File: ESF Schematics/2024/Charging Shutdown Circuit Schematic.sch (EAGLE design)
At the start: 33 parts, among them J1 CONNECTOR-1_6MM2, J10 CONNECTOR-1_CT2242-2, J11 CONNECTOR-5_1-2393947-1, J12 CONNECTOR-3_XXC106-EV-P3Z, J15 CONNECTOR-3_NEMA-5-20, J16 CONNECTOR-3_NEMA-5-20, J17 CONNECTOR-2_, J18 CONNECTOR-2_, J2 CONNECTOR-1_LCAX2-14F-E, J3 CONNECTOR-1_6MM2, J4 CONNECTOR-1_LCAX2-14F-E, J5 CONNECTOR-3_XXC106-EV-P3Z, J6 RING_TERMINAL_19054-0042, J7 RING_TERMINAL_19054-0042, J8 CONNECTOR-3_NEMA-5-20, J9 CONNECTOR-1_CT2242-2

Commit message: num num
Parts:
- removed F3: 175A, HyTechSymbolsTemp:FUSE
- removed F4, F5: 1A, HyTechSymbolsTemp:FUSE
- removed J12, U$3: CONNECTOR-3_XXC106-EV-P3Z, HyTechSymbols:CONNECTOR-3_XXC106-EV-P3Z
- removed J18: CONNECTOR-2_, HyTechSymbols:CONNECTOR-2_XXC104-EV-P1ZA
- removed R1, R2: 15k, HyTechSymbolsTemp:RESISTOR
- removed S2: SWITCH_SPST_, HyTechSymbols:SWITCH_SPST_
- removed U$1, U$4: CONNECTOR-2_HVP800, HyTechSymbols:CONNECTOR-2_HVP800
- removed U$15: CHARGER_CONTROLLER, HyTechSymbolsTemp:CHARGER_CONTROLLER
- removed U$5: BENDER_IR155-3204, HyTechSymbols:BENDER_IR155-3204
- removed U$6: RING_TERMINAL_19054-0042, HyTechSymbolsTemp:RING_TERMINAL_19054-0042
- added AIR+, AIR-: RELAY_SPST_NO_, HyTechSymbols:RELAY_SPST_NO_
- added AMS_RELAY, IMD_RELAY, SOFTWARE_SHDN_RELAY: RELAY_DPDT_RT424024, HyTechSymbols:RELAY_DPDT_RT424024
- added D1, D2, D3, D5, D6, D7: DIODE, HyTechSymbolsTemp:DIODE
- added F1: 3A, HyTechSymbolsTemp:FUSE
- added J14: CONNECTOR-3_NEMA-5-20, HyTechSymbolsTemp:CONNECTOR-3_NEMA-5-20
- added LATCHING_BUTTON: BUTTON_NO_LP9, HyTechSymbolsTemp:BUTTON_NO_LP9
- added S3: SWITCH_SPST_, HyTechSymbols:SWITCH_SPST_
- added U$11: CHARGER_CONTROLLER, HyTechSymbolsTemp:CHARGER_CONTROLLER
- added U$12: BENDER_IR155-3204, HyTechSymbols:BENDER_IR155-3204
- A1: value REMOTE_POWER_CONTROL_RPC-20-SCD -> INLINE_GFCI_GFM20-3WC; device HyTechSymbolsTemp:REMOTE_POWER_CONTROL_RPC-20-SCD -> HyTechSymbolsTemp:INLINE_GFCI_GFM20-3WC
- A2: value CHARGER_HK-J-H650-12 -> REMOTE_POWER_CONTROL_RPC-20-SCD; device HyTechSymbols:CHARGER_HK-J-H650-12 -> HyTechSymbolsTemp:REMOTE_POWER_CONTROL_RPC-20-SCD
- A3: value INLINE_GFCI_GFM20-3WC -> CHARGER_HK-J-H650-12; device HyTechSymbolsTemp:INLINE_GFCI_GFM20-3WC -> HyTechSymbols:CHARGER_HK-J-H650-12
- J10, J9: value CONNECTOR-1_CT2242-2 -> CONNECTOR-3_XXC106-EV-P3Z; device HyTechSymbolsTemp:CONNECTOR-1_CT2242-2 -> HyTechSymbols:CONNECTOR-3_XXC106-EV-P3Z
- J16: value CONNECTOR-3_NEMA-5-20 -> CONNECTOR-2_; device HyTechSymbolsTemp:CONNECTOR-3_NEMA-5-20 -> HyTechSymbols:CONNECTOR-2_XXC104-EV-P1ZA
- J2: value CONNECTOR-1_LCAX2-14F-E -> CONNECTOR-1_6MM2; device HyTechSymbols:CONNECTOR-1_LCAX2-14F-E -> HyTechSymbols:CONNECTOR-1_6MM2
- J3: value CONNECTOR-1_6MM2 -> CONNECTOR-2_HVP800; device HyTechSymbols:CONNECTOR-1_6MM2 -> HyTechSymbols:CONNECTOR-2_HVP800
- J5: value CONNECTOR-3_XXC106-EV-P3Z -> CONNECTOR-2_HVP800; device HyTechSymbols:CONNECTOR-3_XXC106-EV-P3Z -> HyTechSymbols:CONNECTOR-2_HVP800
- J6: value RING_TERMINAL_19054-0042 -> CONNECTOR-1_LCAX2-14F-E; device HyTechSymbols:RING_TERMINAL_19054-0042 -> HyTechSymbols:CONNECTOR-1_LCAX2-14F-E
- J7: value RING_TERMINAL_19054-0042 -> CONNECTOR-3_NEMA-5-20; device HyTechSymbols:RING_TERMINAL_19054-0042 -> HyTechSymbolsTemp:CONNECTOR-3_NEMA-5-20
- J8: value CONNECTOR-3_NEMA-5-20 -> CONNECTOR-3_XXC106-EV-P3Z; device HyTechSymbolsTemp:CONNECTOR-3_NEMA-5-20 -> HyTechSymbols:CONNECTOR-3_XXC106-EV-P3Z
- S1: MPN AIR+ -> CHARGER_SHUTDOWN_BTN
- U$7: value RING_TERMINAL_19054-0042 -> PRECHARGER; device HyTechSymbolsTemp:RING_TERMINAL_19054-0042 -> HyTechSymbolsTemp:PRECHARGER
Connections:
- removed net N$27: R2.1, U$6.P$2
- removed net N$28: A3.HOT_OUT, J8.1
- removed net N$29: A3.GND_OUT, J8.3
- removed net N$30: A3.GND_IN, J16.3
- removed net N$35 (its old number): F4.2, J6.P$2
- removed net N$36 (its old number): F3.2, S2.P
- removed net N$37 (its old number): J11.3, J12.2
- removed net N$9: J10.1, R2.2
- removed net OKHS: U$5.OKHS
- new net AMS_OK: AMS_RELAY.COIL+, D1.C
- new net IMD_OK: D2.C, IMD_RELAY.COIL+, U$12.OKHS
- new net N$13: AIR-.CONTACT2, J5.1, U$7.TS-
- new net N$16: J1.1, J17.1
- new net N$17: J17.2, J2.1
- new net N$18: J10.3, J11.4
- new net N$22: A3.GND, J8.3
- new net N$24: A2.NEUTRAL_IN, J7.2
- new net N$33: A2.GND_OUT, J9.1
- new net N$34: A1.GND_OUT, J14.3
- new net N$40: A3.TS-, J16.2
- new net N$41: J10.1, J11.2
- new net PACK+: AIR+.CONTACT2, U$7.PACK+
- new net PACK-: AIR-.CONTACT1
- new net PRECHARGE_OK: AIR+.COIL-, U$7.PRECHARGE_OK
- new net SOFTWARE_OK: D3.C, SOFTWARE_SHDN_RELAY.COIL+
- net +12V: now also F1.1, U$12.+12V; no longer U$5.+12V
- net CHARGER_CONTROLLER_CANH: now also A3.CANH, U$11.CANH; no longer A2.CANH, U$15.CANH
- net CHARGER_CONTROLLER_CANL: now also A3.CANL, U$11.CANL; no longer A2.CANL, U$15.CANL
- net GND: now also AIR+.COIL+, AIR-.COIL+, AMS_RELAY.4, IMD_RELAY.4, LATCHING_BUTTON.P$2, SOFTWARE_SHDN_RELAY.4, U$12.GND, U$7.GND; no longer U$5.GND
- net N$1: now also D2.A, D7.A, IMD_RELAY.3, IMD_RELAY.COIL-; no longer A2.NEUTRAL, U$3.2
- net N$10: now also AMS_RELAY.5, SOFTWARE_SHDN_RELAY.6; no longer S1.P, U$1.1
- net N$11: now also AMS_RELAY.6, IMD_RELAY.5; no longer F3.1, U$1.2
- net N$12: now also AIR+.CONTACT1, J5.2, U$7.TS+; no longer J11.2, J12.1
- net N$14: now also J3.1, J6.1; no longer J1.1, J18.1
- net N$15: now also A2.HOT_OUT, J9.3; no longer J18.2, J3.1
- net N$19: now also J10.2, J11.3; no longer A1.GND_OUT, J5.3
- net N$2: now also D5.C, D6.C, D7.C, LATCHING_BUTTON.P$1; no longer A2.GND, U$3.3
- net N$20: now also A3.HOT, J8.1; no longer J4.1, U$4.2
- net N$21: now also A3.NEUTRAL, J8.2; no longer J2.1, U$4.1
- net N$23: now also A2.HOTIN, J7.1; no longer A3.NEUTRAL_OUT, J8.2
- net N$25: now also A2.GND_IN, J7.3; no longer R1.1, U$7.P$2
- net N$26: now also A1.HOT_OUT, J14.1; no longer F5.2, J7.P$2
- net N$3: now also AMS_RELAY.3, AMS_RELAY.COIL-, D1.A, D6.A; no longer A2.HOT, U$3.1
- net N$31: now also A1.NEUTRAL_OUT, J14.2; no longer A3.NEUTRAL_IN, J16.2
- net N$32: now also A2.NEUTRAL_OUT, J9.2; no longer A3.HOTIN, J16.1
- net N$39: now also A3.TS+, J16.1; no longer J11.4, J12.3
- net N$4: now also S1.O, S3.P; no longer J17.1
- net N$5: now also D3.A, D5.A, SOFTWARE_SHDN_RELAY.3, SOFTWARE_SHDN_RELAY.COIL-; no longer A2.TS-, J17.2
- net N$6: now also F1.2, IMD_RELAY.6; no longer A1.HOT_OUT, J5.1
- net N$7: now also S1.P, SOFTWARE_SHDN_RELAY.7; no longer A1.NEUTRAL_OUT, J5.2
- net N$8: now also J3.2, J4.1; no longer J9.1, R1.2
- net SHDN: now also A2.EN, AIR-.COIL-, S3.S, U$7.VDD; no longer A1.EN
- net TS+: now also U$12.XLA+(HV+); no longer F4.1, U$5.XLA+(HV+)
- net TS-UNFUSED: now also U$12.XLA-(HV-); no longer F5.1, U$5.XLA-(HV-)
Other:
- note added: "(>= 20 mil)"
- note added: "(Busbar)"
- note added: "ACCUMULATOR"
- note added: "Option 1 for NEMA 5-20"
- note added: "Option 2 for J1772"
- note added: "PCB Trace"
- note added: "PCB Trace:"
- note removed: "25mm^2"
- note removed: "25mm^2:"
- note removed: "Accumulator"
- note removed: "Charger TSMPs"
- note removed: "Direct Connection"
- note removed: "Option 1 for NEMA 5-20:"
- note removed: "Option 2 for J1772:"

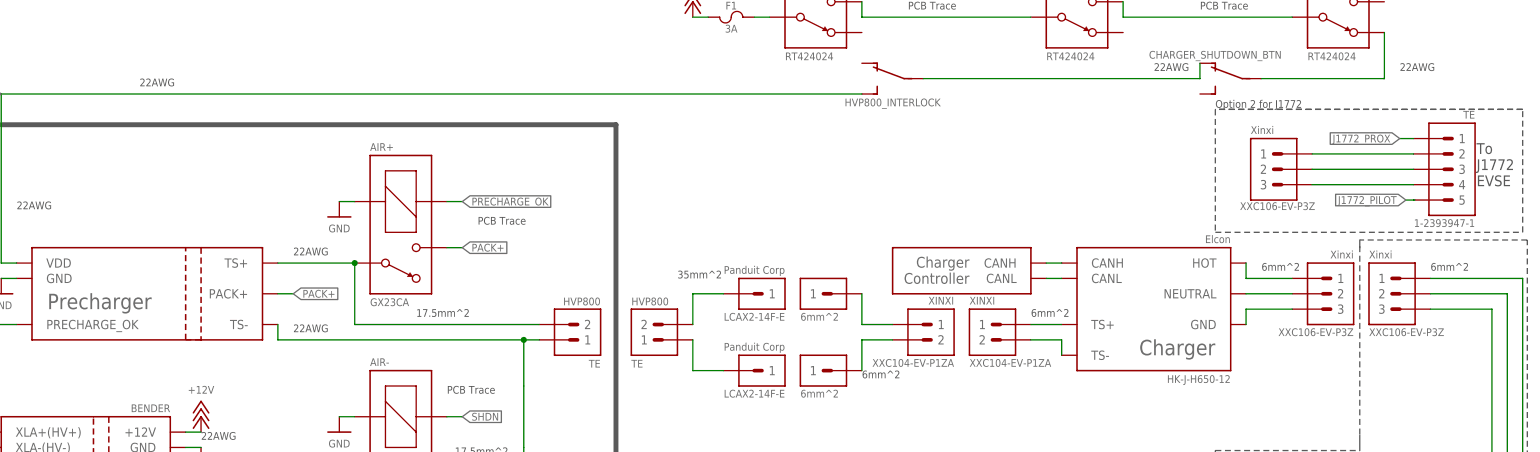
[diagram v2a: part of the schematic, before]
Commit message: changed air+ to be accurate
still need to change precharge stuff
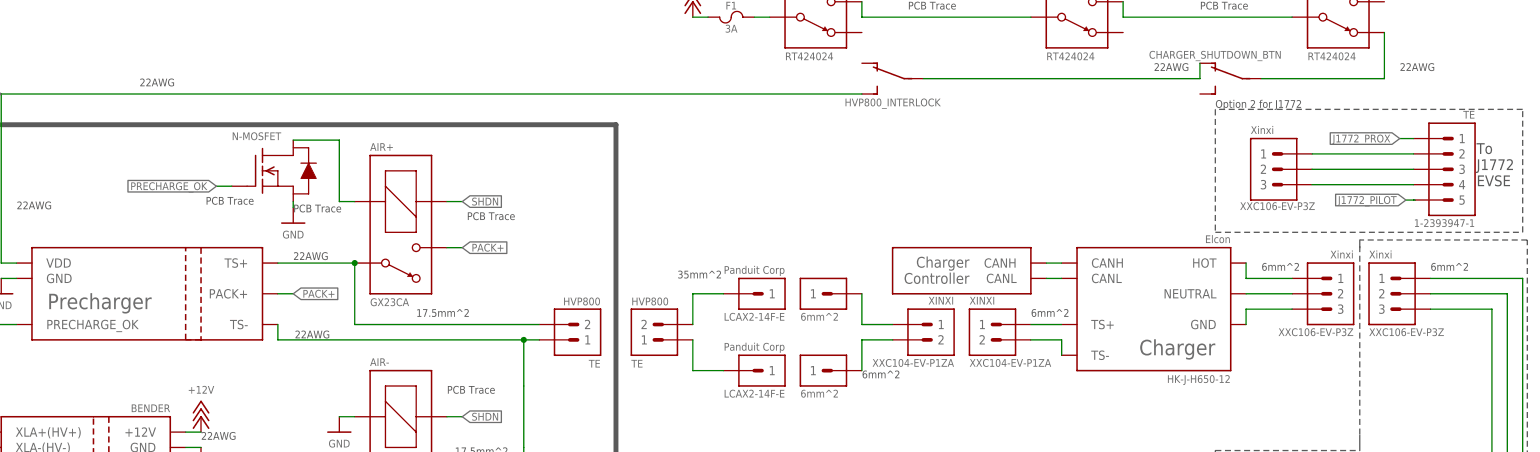
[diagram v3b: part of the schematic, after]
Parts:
- added Q1: MOSFET_N-CHANNEL, HyTechSymbols:MOSFET_N-CHANNEL
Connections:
- new net N$42: AIR+.COIL+, Q1.D
- net GND: now also Q1.S; no longer AIR+.COIL+
- net PRECHARGE_OK: now also Q1.G; no longer AIR+.COIL-
- net SHDN: now also AIR+.COIL-
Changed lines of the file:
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@@
 <part name="J10" library="HyTechSymbols" deviceset="CONNECTOR-3_*" device="" technology="XXC106-EV-P3Z" value="CONNECTOR-3_XXC106-EV-P3Z"/>
 <part name="J11" library="HyTechSymbols" deviceset="CONNECTOR-5_*" device="" technology="1-2393947-1"/>
+<part name="Q1" library="HyTechSymbols" deviceset="MOSFET_N-CHANNEL" device=""/>
 </parts>
 <sheets>
@@
 <text x="236.22" y="58.42" size="1.27" layer="97" rot="MR0" align="top-left">6mm^2</text>
 <text x="25.4" y="119.38" size="1.27" layer="97" align="top-left">22AWG</text>
-<text x="71.12" y="99.06" size="1.27" layer="97" align="top-left">22AWG</text>
-<text x="71.12" y="111.76" size="1.27" layer="97" align="top-left">22AWG</text>
+<text x="71.374" y="98.044" size="1.27" layer="97" align="top-left">22AWG</text>
+<text x="71.12" y="110.998" size="1.27" layer="97" align="top-left">22AWG</text>
 <text x="172.72" y="152.4" size="1.27" layer="97" align="top-left">PCB Trace</text>
 <text x="137.16" y="195.58" size="1.27" layer="97" align="top-left">PCB Trace</text>
@@
 <text x="10.16" y="15.24" size="1.778" layer="97" align="top-left">PCB Trace:</text>
 <text x="25.4" y="12.7" size="1.778" layer="97">(&gt;= 20 mil)</text>
-<text x="101.6" y="116.84" size="1.27" layer="97" align="top-left">PCB Trace</text>
+<text x="99.822" y="117.602" size="1.27" layer="97" align="top-left">PCB Trace</text>
 <text x="96.52" y="88.9" size="1.27" layer="97" align="top-left">PCB Trace</text>
 <text x="17.78" y="81.28" size="1.27" layer="97" rot="MR0" align="top-left">22AWG</text>
@@
 <wire x1="223.52" y1="114.3" x2="274.32" y2="114.3" width="0.1524" layer="97" style="shortdash"/>
 <wire x1="274.32" y1="114.3" x2="274.32" y2="134.62" width="0.1524" layer="97" style="shortdash"/>
-<wire x1="274.32" y1="134.62" x2="223.52" y2="134.62" width="0.1524" layer="97" style="shortdash"/>
 <text x="223.52" y="134.874" size="1.27" layer="97">Option 2 for J1772 </text>
 <wire x1="247.396" y1="112.014" x2="247.396" y2="80.518" width="0.1524" layer="97" style="shortdash"/>
@@
 <wire x1="274.32" y1="134.62" x2="223.52" y2="134.62" width="0.1524" layer="97" style="shortdash"/>
 <text x="131.318" y="71.628" size="1.27" layer="97">Option 1 for NEMA 5-20</text>
+<text x="71.12" y="118.872" size="1.27" layer="97" align="top-left">PCB Trace</text>
+<text x="56.642" y="120.142" size="1.27" layer="97" align="top-left">PCB Trace</text>
 </plain>
 <instances>
@@
 <attribute name="NAME" x="83.82" y="92.202" size="1.27" layer="95"/>
 </instance>
-<instance part="P7" gate="1" x="78.74" y="116.84" smashed="yes">
-<attribute name="VALUE" x="78.74" y="115.57" size="1.27" layer="96" align="top-center"/>
+<instance part="P7" gate="1" x="71.12" y="115.824" smashed="yes">
+<attribute name="VALUE" x="71.12" y="114.554" size="1.27" layer="96" align="top-center"/>
 </instance>
 <instance part="P8" gate="1" x="78.74" y="81.28" smashed="yes">
@@
 <attribute name="MPN" x="266.446" y="116.459" size="1.27" layer="96" rot="MR0" align="top-left"/>
 </instance>
+<instance part="Q1" gate="G$1" x="66.04" y="124.46" smashed="yes"/>
 </instances>
 <busses>
@@
 </segment>
 <segment>
-<pinref part="AIR+" gate="G$1" pin="COIL+"/>
-<wire x1="81.28" y1="119.38" x2="78.74" y2="119.38" width="0.0762" layer="91"/>
-<pinref part="P7" gate="1" pin="GND"/>
-</segment>
-<segment>
 <pinref part="AIR-" gate="G$1" pin="COIL+"/>
 <wire x1="81.28" y1="83.82" x2="78.74" y2="83.82" width="0.0762" layer="91"/>
@@
 <wire x1="53.34" y1="78.74" x2="55.88" y2="78.74" width="0.1524" layer="91"/>
 <pinref part="P10" gate="1" pin="GND"/>
+</segment>
+<segment>
+<pinref part="P7" gate="1" pin="GND"/>
+<pinref part="Q1" gate="G$1" pin="S"/>
+<wire x1="71.12" y1="118.364" x2="71.12" y2="119.38" width="0.0762" layer="91"/>
 </segment>
 </net>
@@
 <pinref part="A2" gate="G$1" pin="EN"/>
 </segment>
+<segment>
+<pinref part="AIR+" gate="G$1" pin="COIL-"/>
+<wire x1="96.52" y1="119.38" x2="99.06" y2="119.38" width="0.0762" layer="91"/>
+<label x="99.06" y="119.38" size="1.27" layer="95" xref="yes"/>
+</segment>
 </net>
 <net name="PACK-" class="0">
@@
 </segment>
 <segment>
-<pinref part="AIR+" gate="G$1" pin="COIL-"/>
-<wire x1="96.52" y1="119.38" x2="99.06" y2="119.38" width="0.0762" layer="91"/>
-<label x="99.06" y="119.38" size="1.27" layer="95" xref="yes"/>
+<pinref part="Q1" gate="G$1" pin="G"/>
+<wire x1="60.96" y1="121.92" x2="58.42" y2="121.92" width="0.0762" layer="91"/>
+<label x="58.42" y="121.92" size="1.27" layer="95" rot="R180" xref="yes"/>
 </segment>
 </net>
@@
 </segment>
 </net>
+<net name="N$42" class="0">
+<segment>
+<pinref part="AIR+" gate="G$1" pin="COIL+"/>
+<wire x1="81.28" y1="119.38" x2="78.74" y2="119.38" width="0.0762" layer="91"/>
+<wire x1="78.74" y1="119.38" x2="78.74" y2="129.54" width="0.0762" layer="91"/>
+<pinref part="Q1" gate="G$1" pin="D"/>
+<wire x1="78.74" y1="129.54" x2="71.12" y2="129.54" width="0.0762" layer="91"/>
+</segment>
+</net>

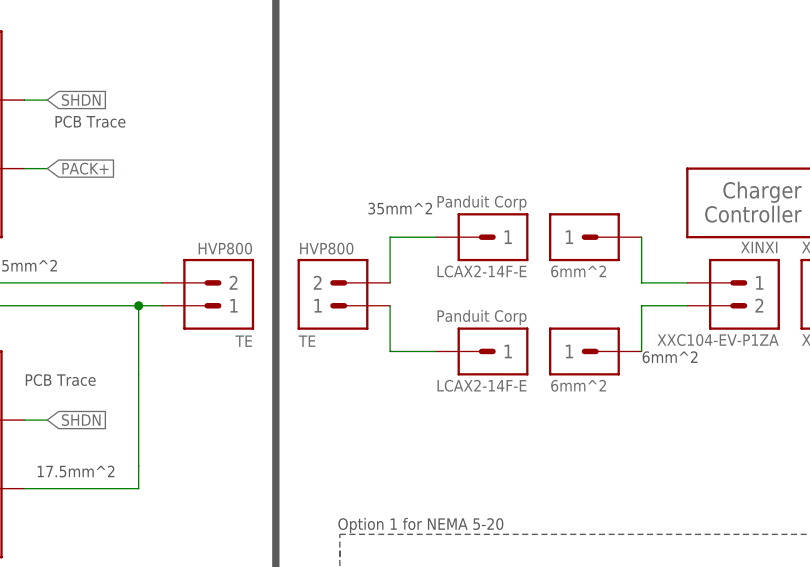
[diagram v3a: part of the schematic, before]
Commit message: Update Charging Shutdown Circuit Schematic.sch
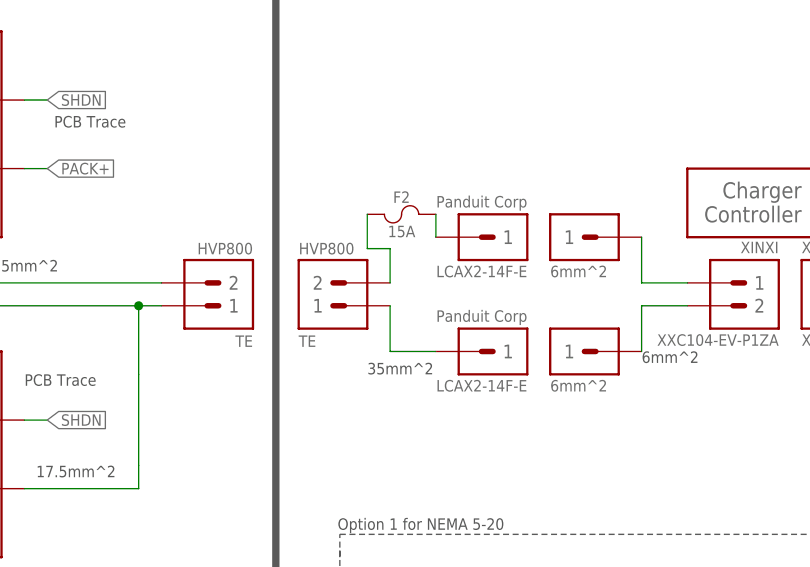
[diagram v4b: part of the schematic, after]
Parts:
- added F2: 15A, HyTechSymbols:FUSE
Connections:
- net N$8: now also F2.1, F2.2
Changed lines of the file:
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@@
 <part name="J11" library="HyTechSymbols" deviceset="CONNECTOR-5_*" device="" technology="1-2393947-1"/>
 <part name="Q1" library="HyTechSymbols" deviceset="MOSFET_N-CHANNEL" device=""/>
+<part name="F2" library="HyTechSymbols" deviceset="FUSE" device="" value="15A"/>
 </parts>
 <sheets>
@@
 AC Power</text>
 <text x="193.04" y="101.6" size="1.27" layer="97" align="top-left">6mm^2</text>
-<text x="134.62" y="106.68" size="1.27" layer="97">35mm^2</text>
+<text x="134.62" y="88.9" size="1.27" layer="97">35mm^2</text>
 <text x="254" y="142.24" size="1.27" layer="97" align="top-left">22AWG</text>
 <text x="45.72" y="139.7" size="1.27" layer="97" align="top-left">22AWG</text>
@@
 </instance>
 <instance part="Q1" gate="G$1" x="66.04" y="124.46" smashed="yes"/>
+<instance part="F2" gate="G$1" x="139.7" y="106.68" smashed="yes">
+<attribute name="NAME" x="138.43" y="107.95" size="1.27" layer="95" align="bottom-center"/>
+<attribute name="VALUE" x="138.43" y="105.41" size="1.27" layer="96" align="top-center"/>
+</instance>
 </instances>
 <busses>
@@
 <net name="N$8" class="0">
 <segment>
+<pinref part="J4" gate="G$1" pin="1"/>
+<wire x1="142.24" y1="106.68" x2="142.24" y2="104.14" width="0.4445" layer="91"/>
+<pinref part="F2" gate="G$1" pin="2"/>
+</segment>
+<segment>
+<wire x1="137.16" y1="102.87" x2="137.16" y2="99.06" width="0.4445" layer="91"/>
 <pinref part="J3" gate="G$1" pin="2"/>
-<pinref part="J4" gate="G$1" pin="1"/>
-<wire x1="137.16" y1="99.06" x2="137.16" y2="104.14" width="0.4445" layer="91"/>
-<wire x1="137.16" y1="104.14" x2="142.24" y2="104.14" width="0.4445" layer="91"/>
-</segment>
-</net>
+<wire x1="134.62" y1="102.87" x2="137.16" y2="102.87" width="0.4445" layer="91"/>
+<wire x1="134.62" y1="106.68" x2="134.62" y2="102.87" width="0.4445" layer="91"/>
+<pinref part="F2" gate="G$1" pin="1"/>
+</segment>
+</net>
